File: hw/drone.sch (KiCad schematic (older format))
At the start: 0 parts

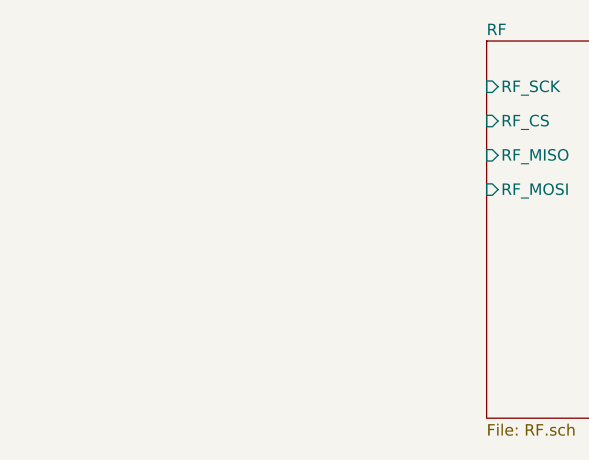
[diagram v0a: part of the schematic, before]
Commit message: Create first revision of IMU sheet assign some footprints.
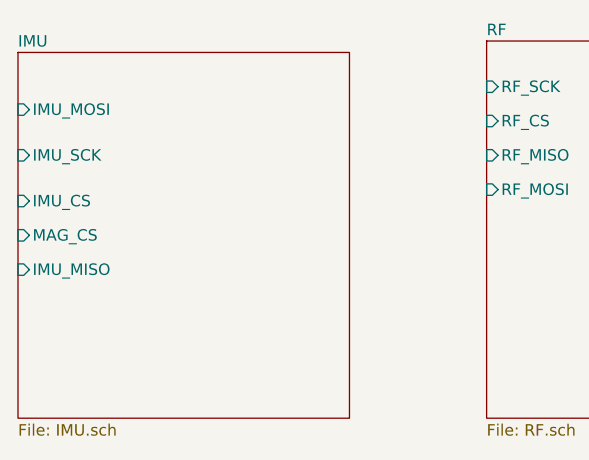
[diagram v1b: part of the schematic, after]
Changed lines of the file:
@@
 EESchema Schematic File Version 4
+LIBS:drone-cache
 EELAYER 30 0
 EELAYER END
 $Descr A4 11693 8268
 encoding utf-8
-Sheet 1 2
+Sheet 1 3
 Title ""
 Date ""
@@
 F5 "RF_MOSI" I L 8550 3250 50
 $EndSheet
+$Sheet
+S 6500 2650 1450 1600
+U 5DAFA187
+F0 "IMU" 50
+F1 "IMU.sch" 50
+F2 "IMU_MOSI" I L 6500 2900 50
+F3 "IMU_SCK" I L 6500 3100 50
+F4 "IMU_CS" I L 6500 3300 50
+F5 "MAG_CS" I L 6500 3450 50
+F6 "IMU_MISO" I L 6500 3600 50
+$EndSheet
 $EndSCHEMATC

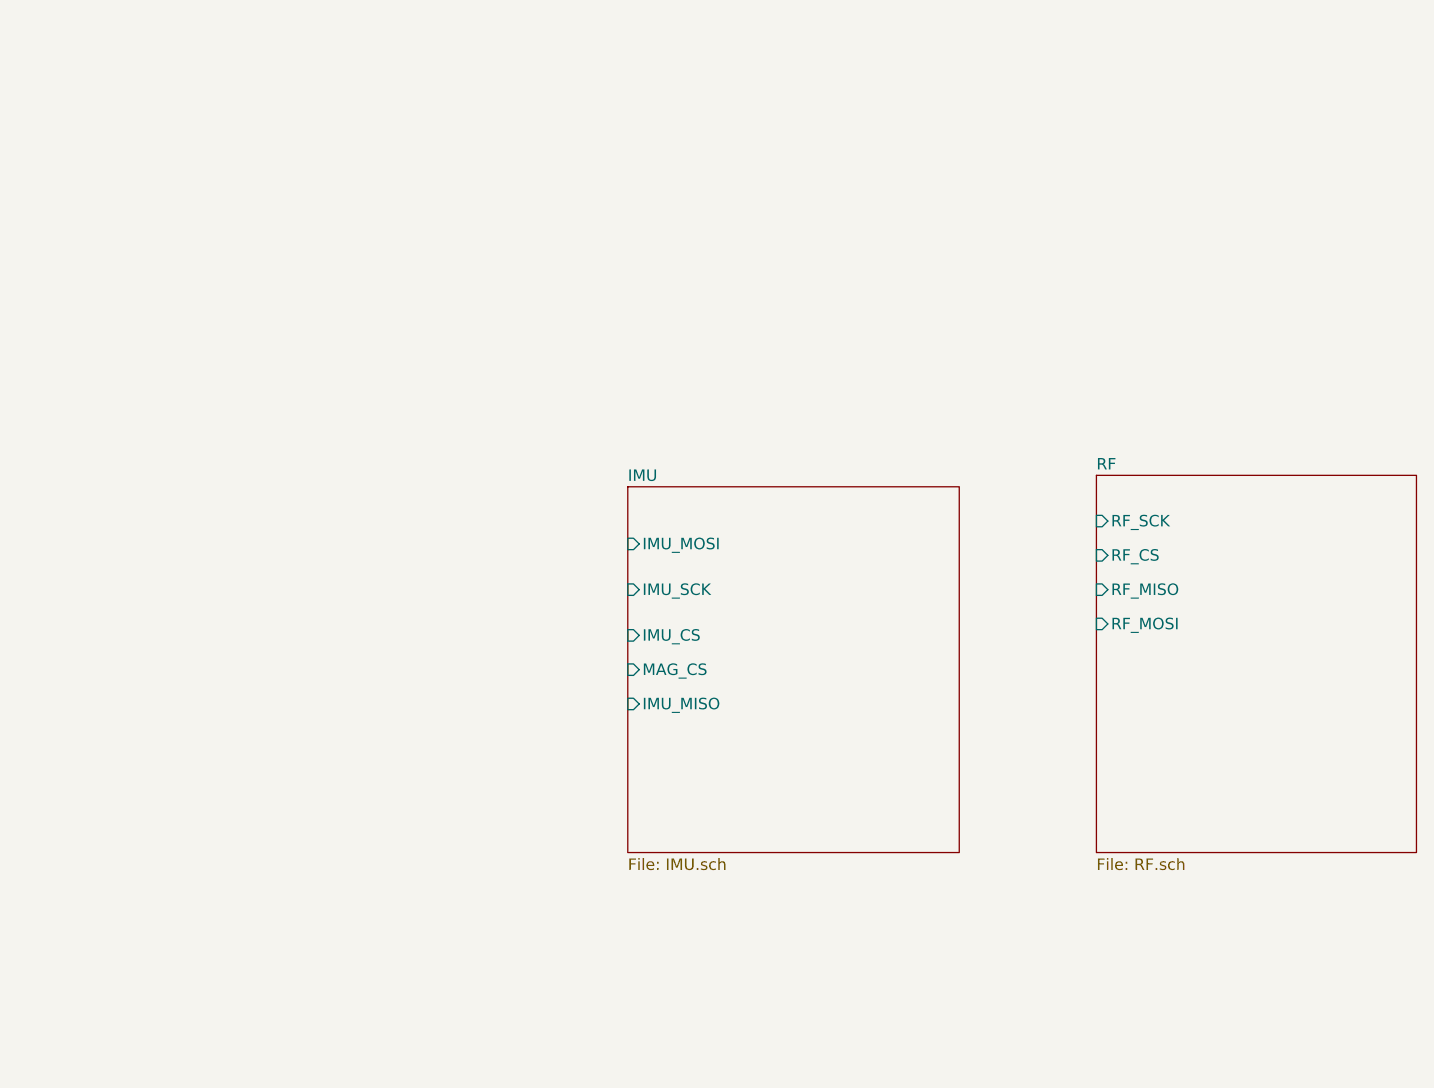
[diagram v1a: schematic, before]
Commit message: Add valid footprints to most schematic symbols. Add pin headers.
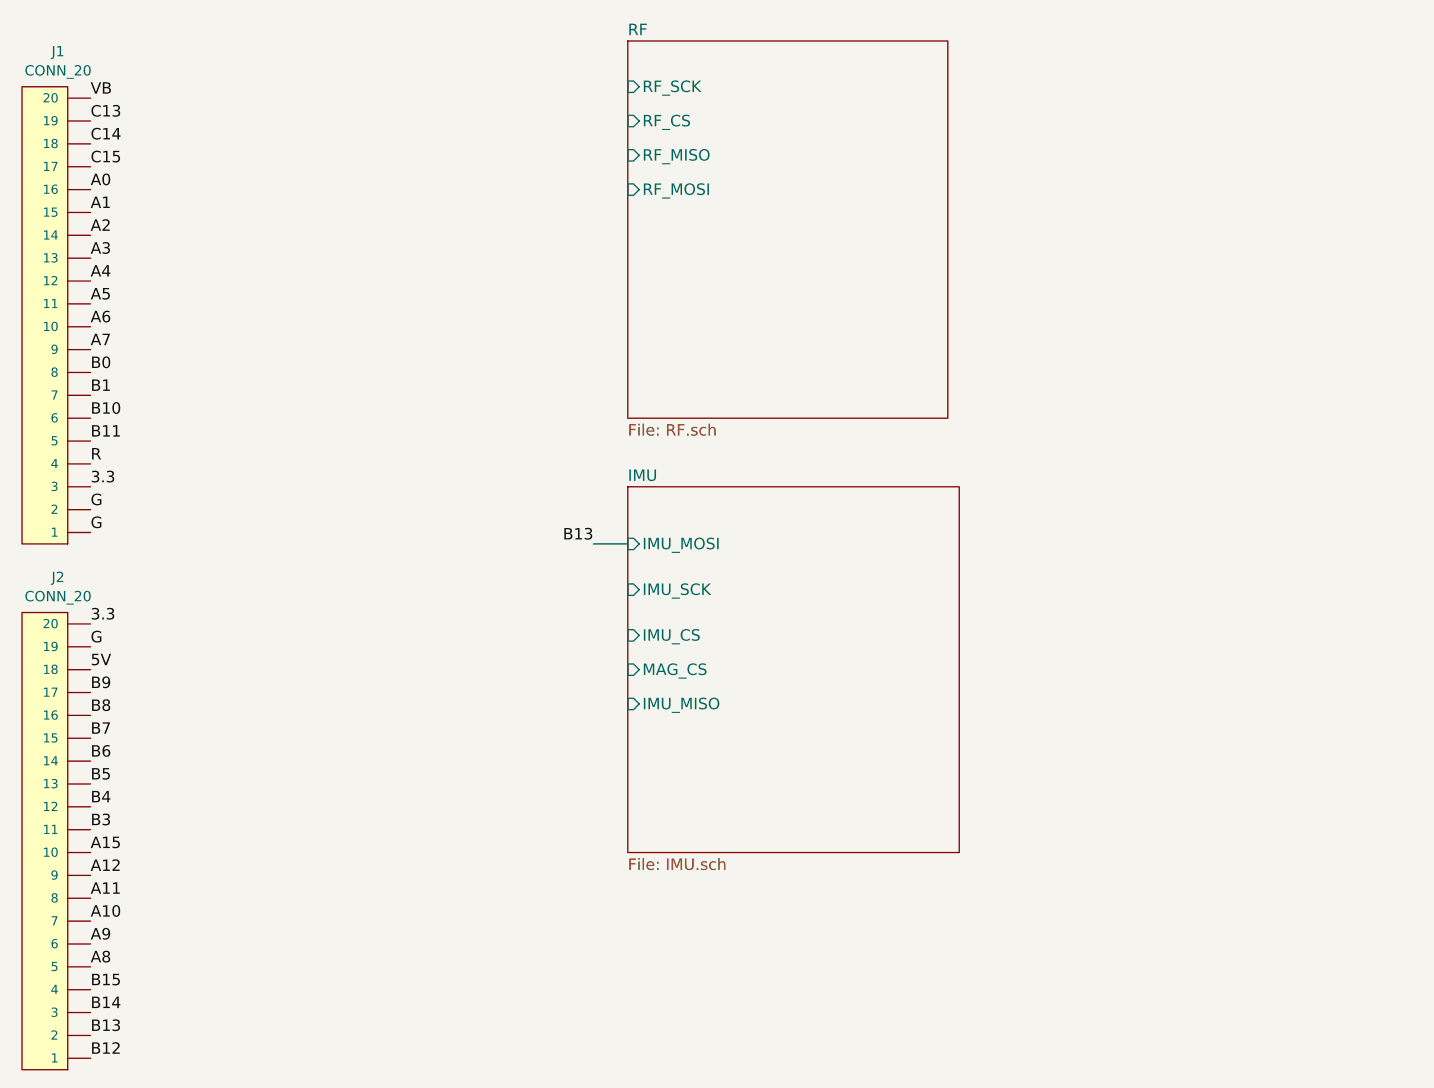
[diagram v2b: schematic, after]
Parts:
- added J1, J2: CONN_20, Connector_PinHeader_2.54mm:PinHeader_1x20_P2.54mm_Vertical, symbol SparkFun-Connectors:CONN_20
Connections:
- new net 3.3: J1.3, J2.20
- new net 5V: J2.18
- new net A0: J1.16
- new net A1: J1.15
- new net A10: J2.7
- new net A11: J2.8
- new net A12: J2.9
- new net A15: J2.10
- new net A2: J1.14
- new net A3: J1.13
- new net A4: J1.12
- new net A5: J1.11
- new net A6: J1.10
- new net A7: J1.9
- new net A8: J2.5
- new net A9: J2.6
- new net B0: J1.8
- new net B1: J1.7
- new net B10: J1.6
- new net B11: J1.5
- new net B12: J2.1
- new net B13: J2.2
- new net B14: J2.3
- new net B15: J2.4
- new net B3: J2.11
- new net B4: J2.12
- new net B5: J2.13
- new net B6: J2.14
- new net B7: J2.15
- new net B8: J2.16
- new net B9: J2.17
- new net C13: J1.19
- new net C14: J1.18
- new net C15: J1.17
- new net G: J1.1, J1.2, J2.19
- new net R: J1.4
- new net VB: J1.20
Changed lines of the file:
@@
 $EndDescr
 $Sheet
-S 8550 2600 1400 1650
+S 6500 700  1400 1650
 U 5D969FF0
 F0 "RF" 50
 F1 "RF.sch" 50
-F2 "RF_SCK" I L 8550 2800 50
-F3 "RF_CS" I L 8550 2950 50
-F4 "RF_MISO" I L 8550 3100 50
-F5 "RF_MOSI" I L 8550 3250 50
+F2 "RF_SCK" I L 6500 900 50
+F3 "RF_CS" I L 6500 1050 50
+F4 "RF_MISO" I L 6500 1200 50
+F5 "RF_MOSI" I L 6500 1350 50
 $EndSheet
 $Sheet
@@
 F6 "IMU_MISO" I L 6500 3600 50
 $EndSheet
+$Comp
+L SparkFun-Connectors:CONN_20 J1
+U 1 1 5DBE5143
+P 4050 2850
+F 0 "J1" H 4008 4954 45  0000 C CNN
+F 1 "CONN_20" H 4008 4870 45  0000 C CNN
+F 2 "Connector_PinHeader_2.54mm:PinHeader_1x20_P2.54mm_Vertical" H 4050 4950 20  0001 C CNN
+F 3 "" H 4050 2850 50  0001 C CNN
+F 4 "XXX-00000" H 4008 4881 60  0001 C CNN "Field4"
+	1    4050 2850
+	1    0    0    -1
+$EndComp
+$Comp
+L SparkFun-Connectors:CONN_20 J2
+U 1 1 5DBE932A
+P 4050 5150
+F 0 "J2" H 4008 7254 45  0000 C CNN
+F 1 "CONN_20" H 4008 7170 45  0000 C CNN
+F 2 "Connector_PinHeader_2.54mm:PinHeader_1x20_P2.54mm_Vertical" H 4050 7250 20  0001 C CNN
+F 3 "" H 4050 5150 50  0001 C CNN
+F 4 "XXX-00000" H 4008 7181 60  0001 C CNN "Field4"
+	1    4050 5150
+	1    0    0    -1
+$EndComp
+Text Label 4150 2850 0    50   ~ 0
+G
+Text Label 4150 2750 0    50   ~ 0
+G
+Text Label 4150 2650 0    50   ~ 0
+3.3
+Text Label 4150 2550 0    50   ~ 0
+R
+Text Label 4150 2450 0    50   ~ 0
+B11
+Text Label 4150 2350 0    50   ~ 0
+B10
+Text Label 4150 2250 0    50   ~ 0
+B1
+Text Label 4150 2150 0    50   ~ 0
+B0
+Text Label 4150 2050 0    50   ~ 0
+A7
+Text Label 4150 1950 0    50   ~ 0
+A6
+Text Label 4150 1850 0    50   ~ 0
+A5
+Text Label 4150 1750 0    50   ~ 0
+A4
+Text Label 4150 1650 0    50   ~ 0
+A3
+Text Label 4150 1550 0    50   ~ 0
+A2
+Text Label 4150 1450 0    50   ~ 0
+A1
+Text Label 4150 1350 0    50   ~ 0
+A0
+Text Label 4150 1250 0    50   ~ 0
+C15
+Text Label 4150 1150 0    50   ~ 0
+C14
+Text Label 4150 1050 0    50   ~ 0
+C13
+Text Label 4150 950  0    50   ~ 0
+VB
+Text Label 4150 3250 0    50   ~ 0
+3.3
+Text Label 4150 3350 0    50   ~ 0
+G
+Text Label 4150 3450 0    50   ~ 0
+5V
+Text Label 4150 3550 0    50   ~ 0
+B9
+Text Label 4150 3650 0    50   ~ 0
+B8
+Text Label 4150 3750 0    50   ~ 0
+B7
+Text Label 4150 3850 0    50   ~ 0
+B6
+Text Label 4150 3950 0    50   ~ 0
+B5
+Text Label 4150 4050 0    50   ~ 0
+B4
+Text Label 4150 4150 0    50   ~ 0
+B3
+Text Label 4150 4250 0    50   ~ 0
+A15
+Text Label 4150 4350 0    50   ~ 0
+A12
+Text Label 4150 4450 0    50   ~ 0
+A11
+Text Label 4150 4550 0    50   ~ 0
+A10
+Text Label 4150 4650 0    50   ~ 0
+A9
+Text Label 4150 4750 0    50   ~ 0
+A8
+Text Label 4150 4850 0    50   ~ 0
+B15
+Text Label 4150 4950 0    50   ~ 0
+B14
+Text Label 4150 5050 0    50   ~ 0
+B13
+Text Label 4150 5150 0    50   ~ 0
+B12
+Text Label 6350 2900 2    50   ~ 0
+B13
+Wire Wire Line
+	6500 2900 6350 2900
 $EndSCHEMATC

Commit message: Partial start to PCB layout.
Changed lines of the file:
@@
 B12
 Text Label 6350 2900 2    50   ~ 0
-B13
+A7
 Wire Wire Line
 	6500 2900 6350 2900
+Text Label 6350 3600 2    50   ~ 0
+A6
+Text Label 6350 3100 2    50   ~ 0
+A5
+Wire Wire Line
+	6350 3100 6500 3100
+Wire Wire Line
+	6350 3600 6500 3600
+Text Label 6350 3300 2    50   ~ 0
+A3
+Text Label 6350 3450 2    50   ~ 0
+A2
+Wire Wire Line
+	6350 3300 6500 3300
+Wire Wire Line
+	6350 3450 6500 3450
 $EndSCHEMATC
